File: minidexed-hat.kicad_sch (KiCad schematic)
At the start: 5 parts, among them J1 RPi_GPIO

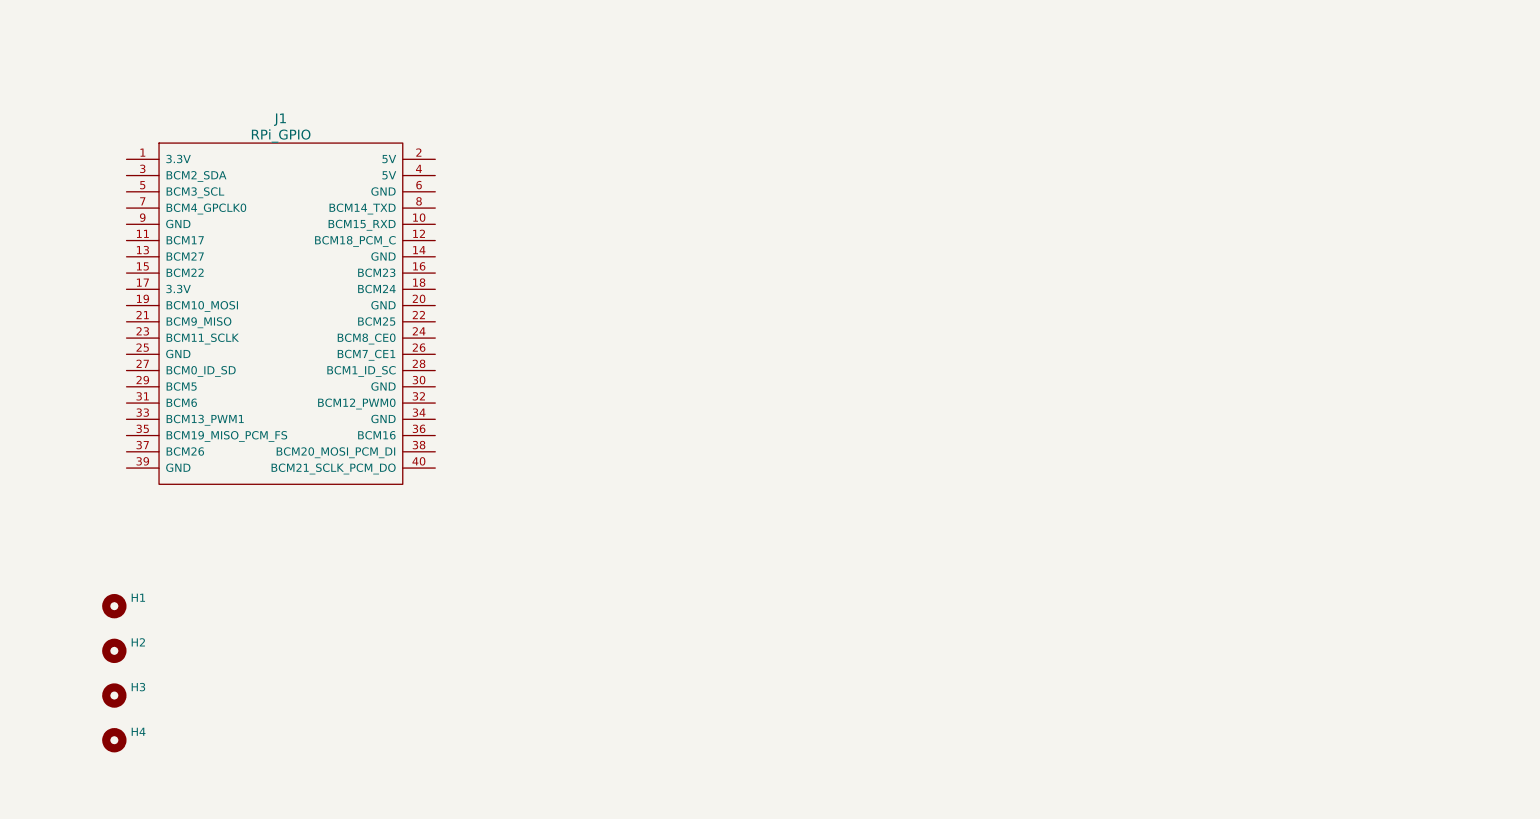
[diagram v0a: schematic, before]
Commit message: Complete with MIDI and connectors off-board
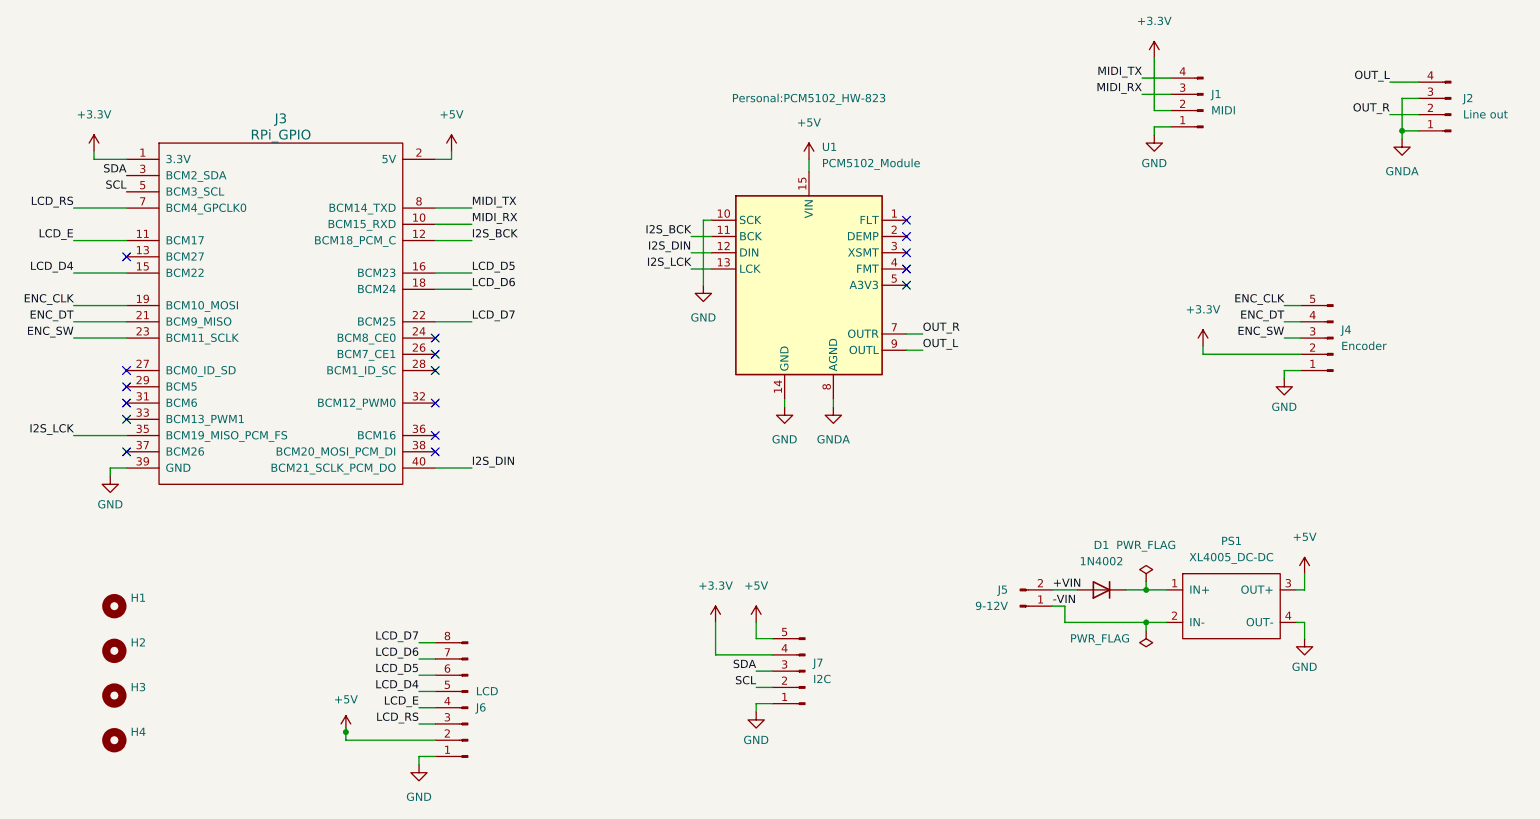
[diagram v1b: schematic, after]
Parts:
- added D1: 1N4002, Diode_THT:D_DO-41_SOD81_P10.16mm_Horizontal, symbol Diode:1N4002
- added J1: MIDI, Connector_PinHeader_2.54mm:PinHeader_1x04_P2.54mm_Vertical, symbol Connector:Conn_01x04_Male
- added J2: Line out, Connector_PinHeader_2.54mm:PinHeader_1x04_P2.54mm_Vertical, symbol Connector:Conn_01x04_Male
- added J4: Encoder, Connector_PinHeader_2.54mm:PinHeader_1x05_P2.54mm_Vertical, symbol Connector:Conn_01x05_Male
- added J5: 9-12V, Connector_PinHeader_2.54mm:PinHeader_1x02_P2.54mm_Vertical, symbol Connector:Conn_01x02_Male
- added J6: LCD, Connector_PinHeader_2.54mm:PinHeader_1x08_P2.54mm_Vertical, symbol Connector:Conn_01x08_Male
- added J7: I2C, Connector_PinHeader_2.54mm:PinHeader_1x05_P2.54mm_Vertical, symbol Connector:Conn_01x05_Male
- added PS1: XL4005_DC-DC, Personal:XL4005_DC-DC, symbol Personal:XL4005_DC-DC
- added U1: PCM5102_Module, Personal:PCM5102_HW-823, symbol Personal:PCM5102_HW-823
- H1, H2, H3, H4: value (none) -> ~
- J3: renamed from J1; footprint RPi_Hat:Pin_Header_Straight_2x20 -> Connector_PinSocket_2.54mm:PinSocket_2x20_P2.54mm_Vertical; symbol RPi_Hat:RPi_GPIO -> Personal:RPi_GPIO
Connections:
- net +3.3V: now reaches J3.1 (3.3V)
- net +3.3V: now also J3.17 (3.3V), J1.2 (Pin_2), J4.2 (Pin_2), J7.4 (Pin_4)
- net MIDI_RX: now reaches J3.10 (BCM15_RXD)
- net MIDI_RX: now also J1.3 (Pin_3)
- net LCD_E: now reaches J3.11 (BCM17)
- net LCD_E: now also J6.4 (Pin_4)
- net I2S_BCK: now reaches J3.12 (BCM18_PCM_C)
- net I2S_BCK: now also U1.11 (BCK)
- net GND: now reaches J3.14 (GND)
- net GND: now also J3.20 (GND), J3.25 (GND), J3.30 (GND), J3.34 (GND), J3.39 (GND), J3.6 (GND), J3.9 (GND), J1.1 (Pin_1), J4.1 (Pin_1), J6.1 (Pin_1), J7.1 (Pin_1), PS1.4 (OUT-), U1.10 (SCK), U1.14 (GND)
- net LCD_D4: now reaches J3.15 (BCM22)
- net LCD_D4: now also J6.5 (Pin_5)
- net LCD_D5: now reaches J3.16 (BCM23)
- net LCD_D5: now also J6.6 (Pin_6)
- net LCD_D6: now reaches J3.18 (BCM24)
- net LCD_D6: now also J6.7 (Pin_7)
- net ENC_CLK: now reaches J3.19 (BCM10_MOSI)
- net ENC_CLK: now also J4.5 (Pin_5)
- net +5V: now reaches J3.2 (5V)
- net +5V: now also J3.4 (5V), J6.2 (Pin_2), J7.5 (Pin_5), PS1.3 (OUT+), U1.15 (VIN)
- net ENC_DT: now reaches J3.21 (BCM9_MISO)
- net ENC_DT: now also J4.4 (Pin_4)
- net LCD_D7: now reaches J3.22 (BCM25)
- net LCD_D7: now also J6.8 (Pin_8)
- net ENC_SW: now reaches J3.23 (BCM11_SCLK)
- net ENC_SW: now also J4.3 (Pin_3)
- net SDA: now reaches J3.3 (BCM2_SDA)
- net SDA: now also J7.3 (Pin_3)
- net I2S_LCK: now reaches J3.35 (BCM19_MISO_PCM_FS)
- net I2S_LCK: now also U1.13 (LCK)
- net I2S_DIN: now reaches J3.40 (BCM21_SCLK_PCM_DO)
- net I2S_DIN: now also U1.12 (DIN)
- net SCL: now reaches J3.5 (BCM3_SCL)
- net SCL: now also J7.2 (Pin_2)
- net LCD_RS: now reaches J3.7 (BCM4_GPCLK0)
- net LCD_RS: now also J6.3 (Pin_3)
- net MIDI_TX: now reaches J3.8 (BCM14_TXD)
- net MIDI_TX: now also J1.4 (Pin_4)
- new net: D1.1 (K), PS1.1 (IN+)
- new net +VIN: D1.2 (A), J5.2 (Pin_2)
- new net -VIN: J5.1 (Pin_1), PS1.2 (IN-)
- new net GNDA: J2.1 (Pin_1), J2.3 (Pin_3), U1.6 (AGND), U1.8 (AGND)
- new net OUT_L: J2.4 (Pin_4), U1.9 (OUTL)
- new net OUT_R: J2.2 (Pin_2), U1.7 (OUTR)
- no-connect marks 0 -> 17
